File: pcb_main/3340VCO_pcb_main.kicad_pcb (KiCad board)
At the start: 2 copper layers, 80 x 114.5 mm, 75 parts, among them J1 MJ-352, J2 MJ-352, J3 MJ-352, J4 POWER_IN, J5 MJ-352, J6 MJ-352, J7 MJ-352, U1 NJM074, U2 NJM074, U3 V3340M

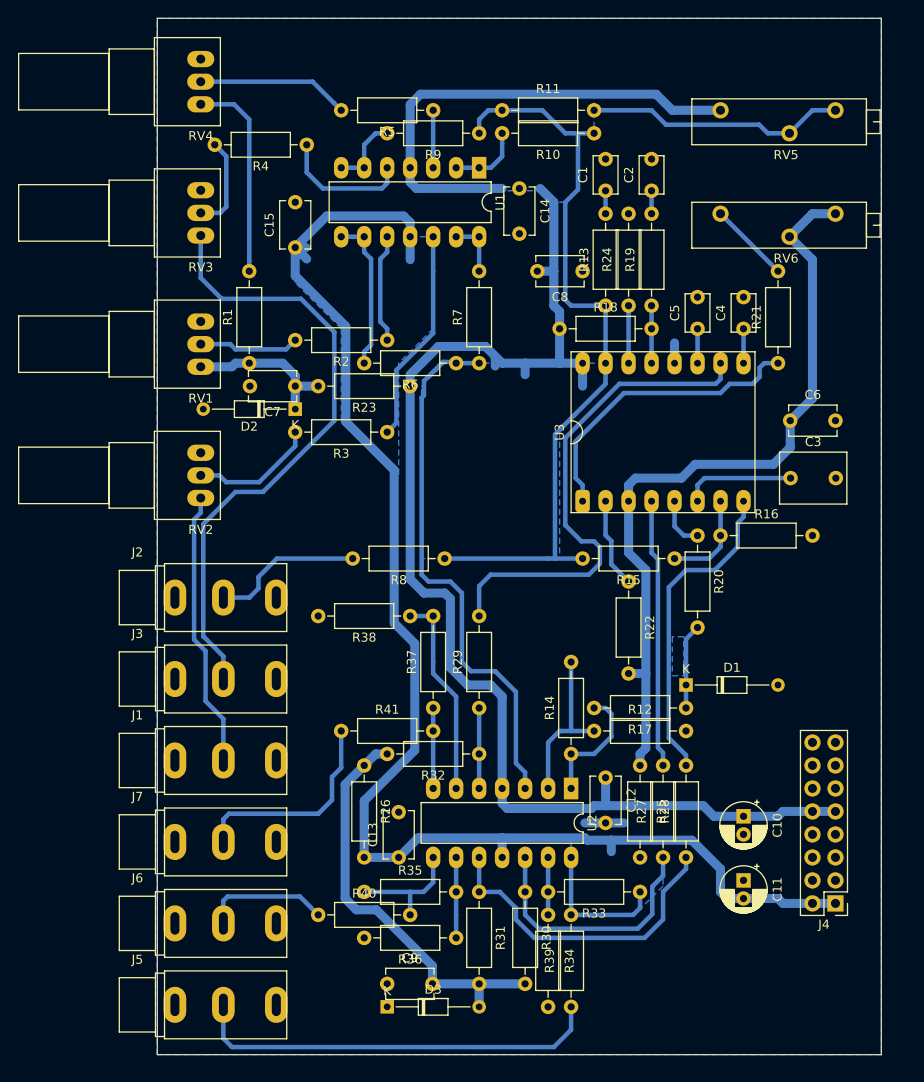
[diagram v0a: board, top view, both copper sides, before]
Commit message: pcb_main modify height: 114.5->109.5mm, optimize pad/drill diameter
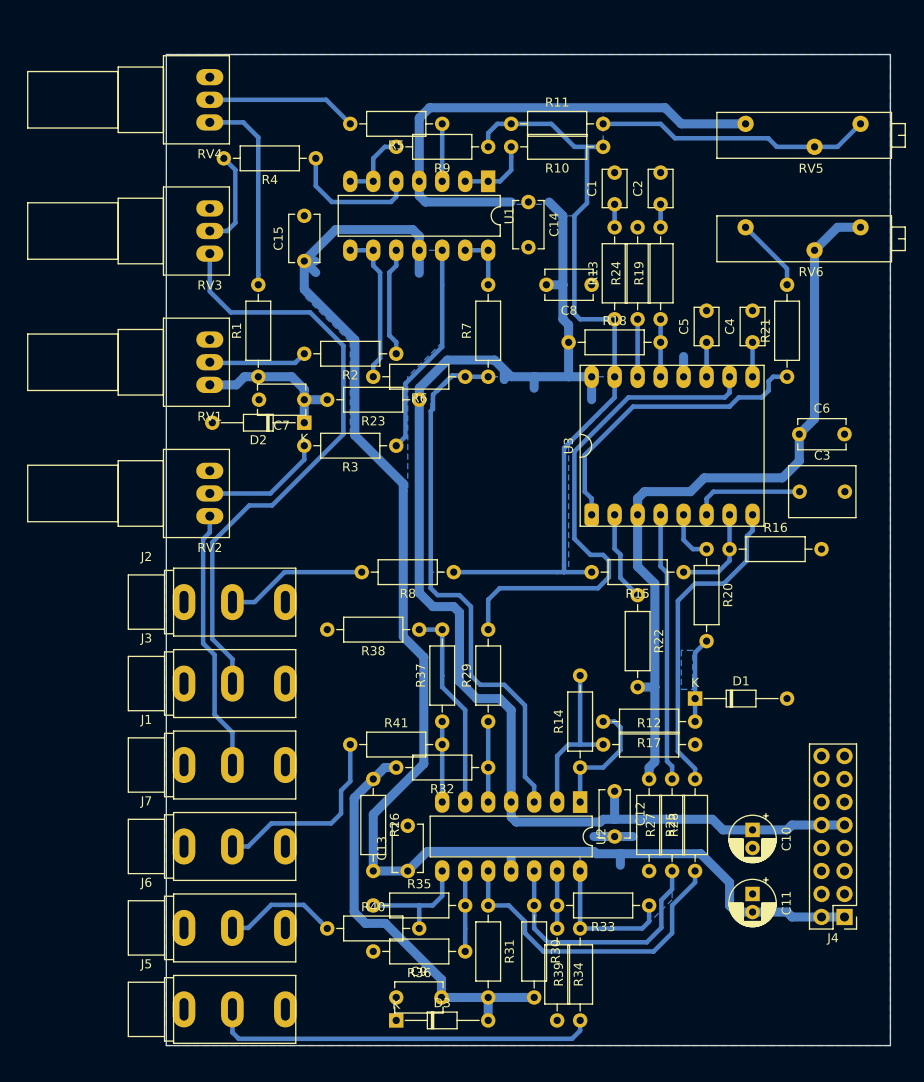
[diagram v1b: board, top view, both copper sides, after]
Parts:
- moved RV5 3.15 mm to (115.0, 61.7)
- moved RV6 3.15 mm to (115.0, 73.1)
- moved RV1 2.24 mm to (55.8, 85.5)
- moved RV2 2.24 mm to (55.8, 100.0)
- moved RV3 2.24 mm to (55.8, 71.0)
- moved RV4 2.24 mm to (55.8, 56.5)
- moved C1 1.80 mm to (100.5, 70.0)
- moved C10 1.80 mm to (115.8, 139.7)
- moved C11 1.80 mm to (115.8, 146.8)
- moved C12 1.80 mm to (100.5, 135.4)
- moved C13 1.80 mm to (77.7, 144.2)
- moved C14 1.80 mm to (91.0, 70.3)
- moved C15 1.80 mm to (66.2, 76.8)
- moved C2 1.80 mm to (105.6, 70.0)
- moved C3 1.80 mm to (121.0, 102.3)
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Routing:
- net Net-(J5-PadT): track 45.9 -> 42.8 mm
- net Net-(J7-PadT): track 23.4 -> 21.6 mm
- net Net-(J3-PadT): track 68.9 -> 67.1 mm
- net +12V: track 197.8 -> 199.5 mm
- net Net-(R11-Pad2): track 28.8 -> 30.5 mm
- net Net-(J1-PadT): track 30.6 -> 29.1 mm
- net Net-(J6-PadT): track 14.0 -> 12.6 mm
- net /VCO_VEE: track 85.0 -> 83.6 mm
- net Net-(J2-PadT): track 16.8 -> 15.7 mm
- net Net-(R21-Pad2): track 8.98 -> 8.25 mm
- net Net-(R4-Pad2): track 10.3 -> 10.9 mm
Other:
- board size 80 x 114.5 mm -> 80 x 109.5 mm

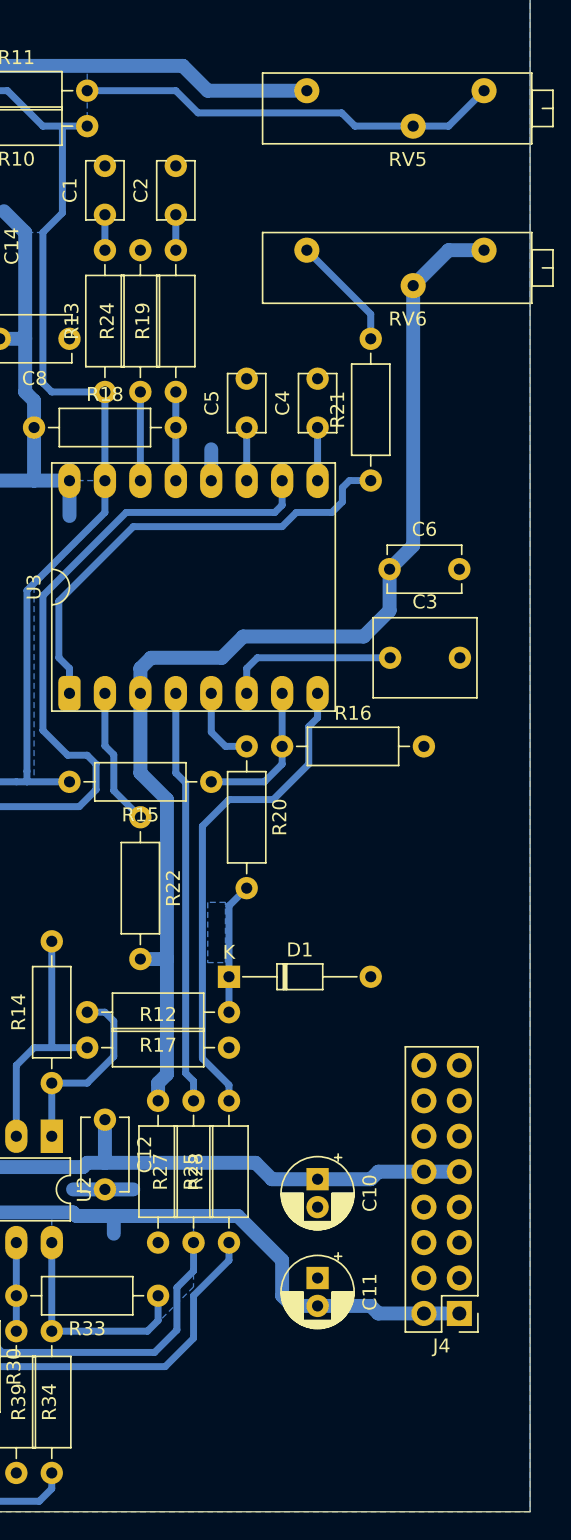
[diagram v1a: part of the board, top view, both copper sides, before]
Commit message: flip RV5 pin assign, add power source protection diode
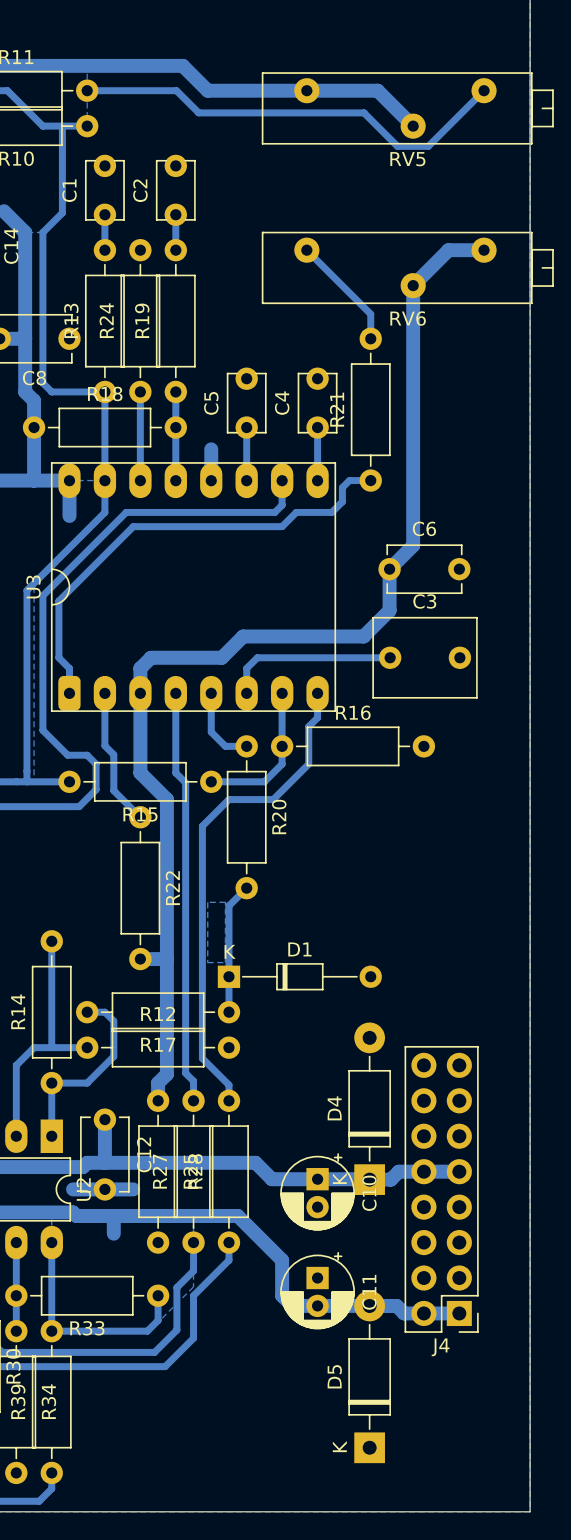
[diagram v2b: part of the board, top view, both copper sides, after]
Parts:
- added D4: 1N4007, Diode_THT:D_DO-41_SOD81_P10.16mm_Horizontal, F.Cu at (119.5, 139.7)
- added D5: 1N4007, Diode_THT:D_DO-41_SOD81_P10.16mm_Horizontal, F.Cu at (119.5, 158.9)
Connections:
- RV5 pad 2: Net-(R11-Pad2) -> +12V
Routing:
- net +12V: track 199.5 -> 208.2 mm
- net Net-(R11-Pad2): track 30.5 -> 31.7 mm

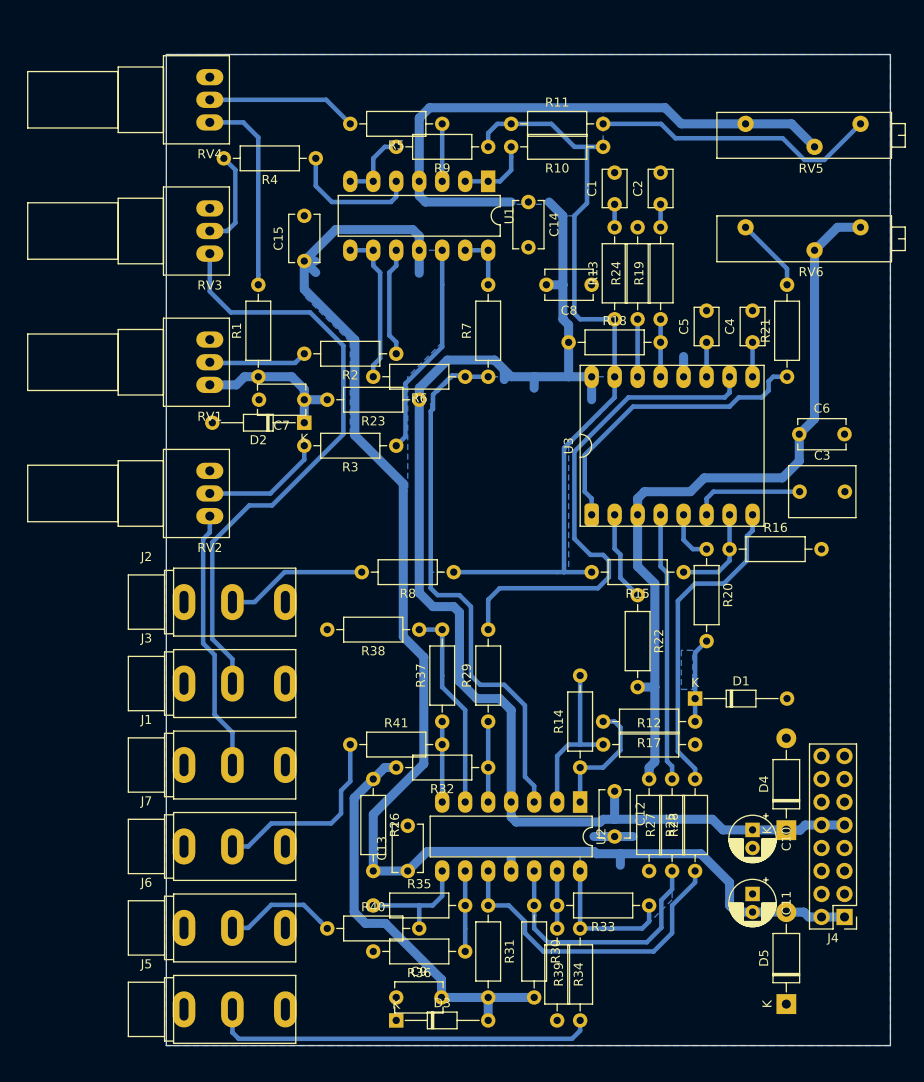
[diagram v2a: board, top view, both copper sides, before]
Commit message: redesign pcb_main for double-side
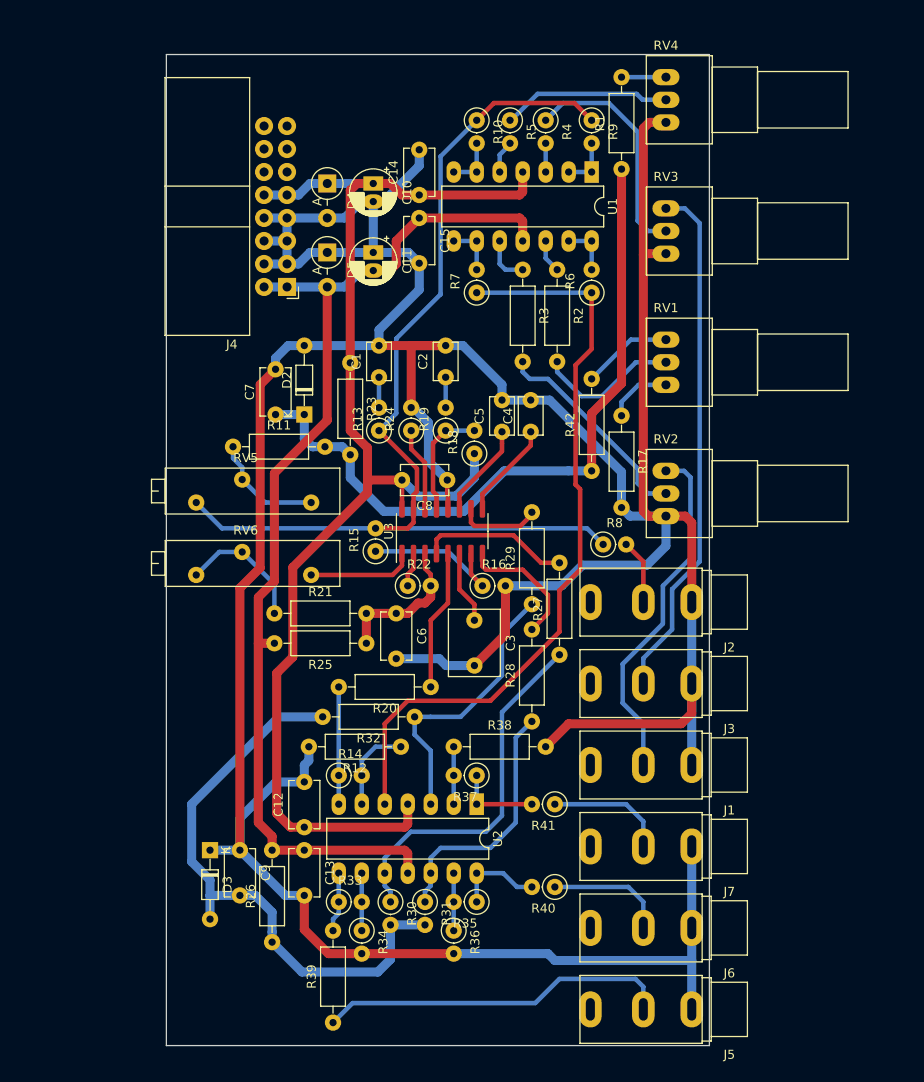
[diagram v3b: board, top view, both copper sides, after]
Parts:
- removed D1: 1N5231B, Diode_THT:D_DO-34_SOD68_P10.16mm_Horizontal
- added R42: 27k, Resistor_THT:R_Axial_DIN0207_L6.3mm_D2.5mm_P10.16mm_Horizontal, F.Cu at (98.0, 100.0)
- D2, D3: footprint Diode_THT:D_DO-34_SOD68_P10.16mm_Horizontal -> Diode_THT:D_DO-34_SOD68_P7.62mm_Horizontal
- D4, D5: footprint Diode_THT:D_DO-41_SOD81_P10.16mm_Horizontal -> Diode_THT:D_DO-41_SOD81_P3.81mm_Vertical_AnodeUp
- J4: footprint Connector_PinHeader_2.54mm:PinHeader_2x08_P2.54mm_Vertical -> Connector_IDC:IDC-Header_2x08_P2.54mm_Horizontal
- R10, R13, R14, R15, R16, R18, R19, R22, R24, R30, R31, R33, R34, R35, R36, R37, R4, R40, R41, R5, R6, R7, R8, R9: footprint Resistor_THT:R_Axial_DIN0207_L6.3mm_D2.5mm_P10.16mm_Horizontal -> Resistor_THT:R_Axial_DIN0207_L6.3mm_D2.5mm_P2.54mm_Vertical
- R11: value 200k -> 82k
- R17: value 1k -> 1.5k
- R25: value 820 -> 510
- R29: value 39k -> 3.9k
- RV5: value 100k -> 50k
- U3: footprint sop_conv:sop_conv_16pin -> Package_SO:SOIC-16_3.9x9.9mm_P1.27mm
- moved D5 97.3 mm to (68.8, 75.9), turned to 270 degrees
- moved J4 92.9 mm to (64.3, 79.7)
- moved D4 87.6 mm to (68.8, 68.2), turned to 270 degrees
- moved C10 82.8 mm to (73.9, 68.2)
- moved C11 82.3 mm to (73.9, 75.9)
- moved J1 68.4 mm to (115.2, 132.5), turned to 180 degrees
- moved J2 68.4 mm to (115.2, 114.5), turned to 180 degrees
- moved J3 68.4 mm to (115.2, 123.5), turned to 180 degrees
- moved J5 68.4 mm to (115.2, 159.5), turned to 180 degrees
- moved J6 68.4 mm to (115.2, 150.5), turned to 180 degrees
- moved J7 68.4 mm to (115.2, 141.5), turned to 180 degrees
- moved RV5 63.7 mm to (67.0, 103.5), turned to 0 degrees
- moved R21 62.4 mm to (62.9, 115.7), turned to 0 degrees
- moved RV6 61.5 mm to (67.0, 111.5), turned to 0 degrees
- moved RV1 50.6 mm to (106.2, 90.5), turned to 0 degrees
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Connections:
- C6 pad 1: /VCO_VEE -> VEE
- R11 pad 1: Net-(R10-Pad1) -> Net-(R11-Pad1)
- R11 pad 2: Net-(R11-Pad2) -> +5V
- R17 pad 1: Net-(D1-Pad1) -> Net-(R17-Pad1)
- R17 pad 2: Net-(R14-Pad1) -> GND
- R20 pad 2: Net-(D1-Pad1) -> Net-(R14-Pad1)
- R21 pad 2: Net-(R21-Pad2) -> VEE
- R22 pad 2: /VCO_VEE -> VEE
- R25 pad 1: /VCO_VEE -> VEE
- RV1 pad 1: GND -> Net-(R17-Pad1)
- RV1 pad 3: +5V -> Net-(R42-Pad2)
- RV3 pad 2: Net-(R4-Pad2) -> Net-(R4-Pad1)
- RV4 pad 2: Net-(R5-Pad2) -> Net-(R5-Pad1)
- RV5 pad 1: +12V -> Net-(R11-Pad1)
- RV5 pad 2: +12V -> Net-(R11-Pad1)
- RV5 pad 3: Net-(R11-Pad2) -> Net-(R10-Pad1)
- RV6 pad 1: Net-(R21-Pad2) -> Net-(RV6-Pad1)
- RV6 pad 2: /VCO_VEE -> Net-(R21-Pad1)
- RV6 pad 3: /VCO_VEE -> Net-(R21-Pad1)
- U1 pad 1: Net-(R10-Pad2) -> Net-(R9-Pad2)
- U1 pad 10: Net-(R2-Pad1) -> Net-(R3-Pad1)
- U1 pad 12: Net-(R3-Pad1) -> Net-(R2-Pad1)
- U1 pad 13: Net-(R7-Pad2) -> Net-(R6-Pad2)
- U1 pad 14: Net-(R7-Pad2) -> Net-(R6-Pad2)
- U1 pad 2: Net-(R10-Pad2) -> Net-(R9-Pad2)
- U1 pad 3: Net-(R5-Pad1) -> Net-(R4-Pad2)
- U1 pad 5: Net-(R4-Pad1) -> Net-(R5-Pad2)
- U1 pad 6: Net-(R9-Pad2) -> Net-(R10-Pad2)
- U1 pad 7: Net-(R9-Pad2) -> Net-(R10-Pad2)
- U1 pad 8: Net-(R6-Pad2) -> Net-(R7-Pad2)
- U1 pad 9: Net-(R6-Pad2) -> Net-(R7-Pad2)
- U2 pad 1: Net-(R14-Pad1) -> Net-(R37-Pad1)
- U2 pad 10: Net-(R28-Pad1) -> Net-(R27-Pad1)
- U2 pad 12: Net-(R27-Pad1) -> Net-(R28-Pad1)
- U2 pad 13: Net-(R33-Pad2) -> Net-(R35-Pad2)
- U2 pad 14: Net-(R33-Pad1) -> Net-(R35-Pad1)
- U2 pad 2: Net-(R12-Pad1) -> Net-(R37-Pad2)
- U2 pad 3: Net-(R6-Pad1) -> Net-(R29-Pad1)
- U2 pad 5: Net-(R29-Pad1) -> Net-(R6-Pad1)
- U2 pad 6: Net-(R37-Pad2) -> Net-(R12-Pad1)
- U2 pad 7: Net-(R37-Pad1) -> Net-(R14-Pad1)
- U2 pad 8: Net-(R35-Pad1) -> Net-(R33-Pad1)
- U2 pad 9: Net-(R35-Pad2) -> Net-(R33-Pad2)
- U3 pad 1: Net-(R21-Pad1) -> Net-(RV6-Pad1)
- U3 pad 3: /VCO_VEE -> VEE
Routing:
- net GND: track 6.57 -> 436.1 mm
- net /VCO_VEE: track 83.6 -> 0.00 mm
- net +12V: track 208.2 -> 145.4 mm
- net +5V: track 17.6 -> 79.0 mm
- net Net-(R29-Pad2): track 55.6 -> 9.19 mm
- net -12V: track 157.7 -> 120.7 mm
- net Net-(R11-Pad2): track 31.7 -> 0.00 mm
- net Net-(R10-Pad1): track 84.9 -> 116.4 mm
- net Net-(R6-Pad1): track 59.8 -> 84.5 mm
- net Net-(R29-Pad1): track 8.89 -> 31.2 mm
- net Net-(R28-Pad2): track 35.3 -> 14.5 mm
- net -5V: track 46.1 -> 65.6 mm
- net Net-(R21-Pad1): track 33.5 -> 14.4 mm
- net Net-(R3-Pad1): track 23.7 -> 5.34 mm
- net Net-(R1-Pad2): track 22.3 -> 4.91 mm
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- removed copper zone on B.Cu, net +12V
- removed copper zone on B.Cu, net -12V
- removed copper zone on B.Cu, net GND
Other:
- board size 80 x 109.5 mm -> 60 x 109.5 mm

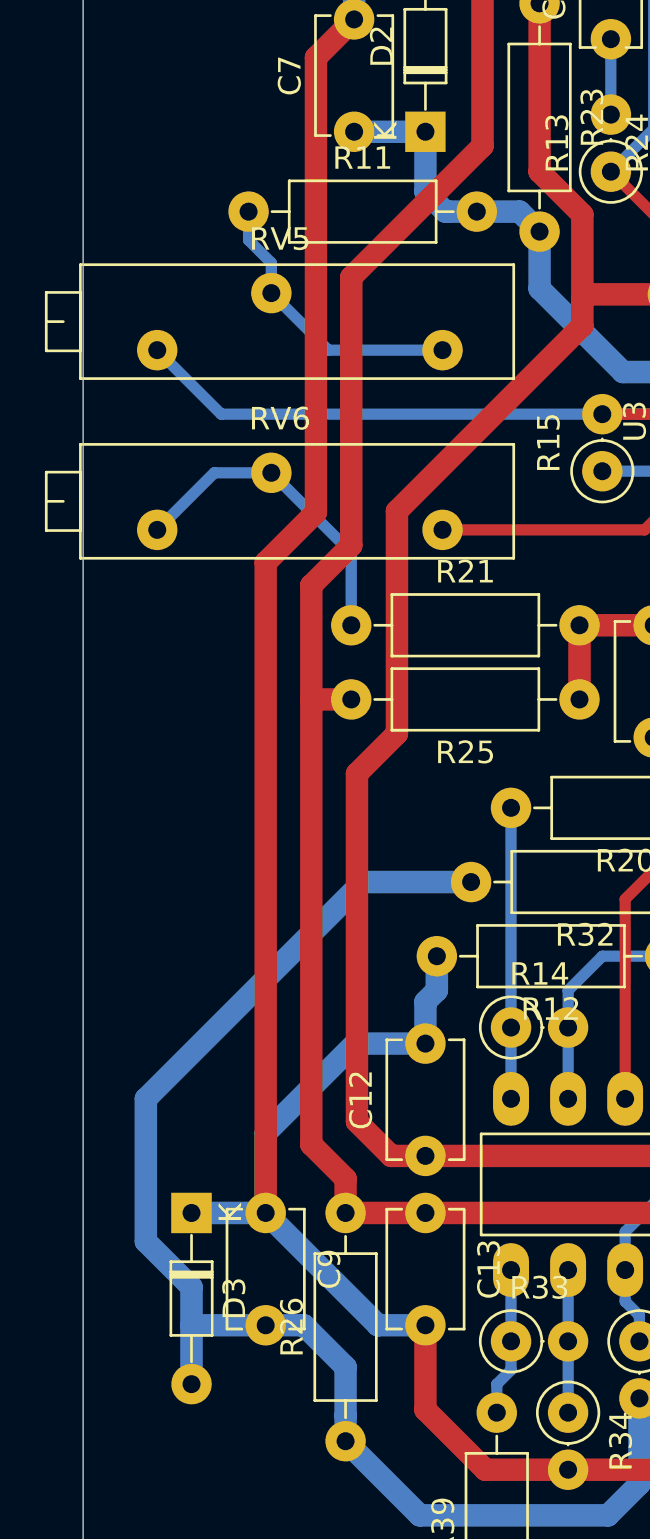
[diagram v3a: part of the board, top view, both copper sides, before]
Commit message: tweak pcb_main, adjust frontpanel horizontal position
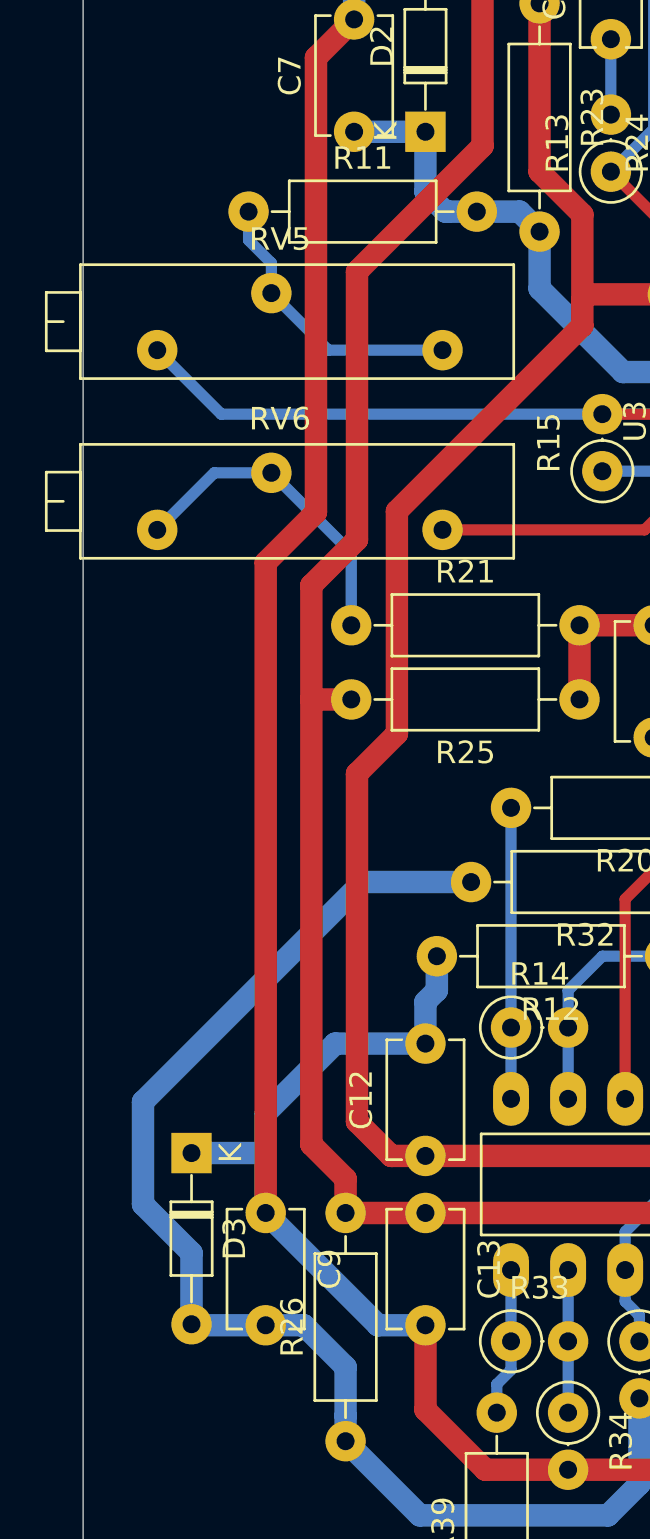
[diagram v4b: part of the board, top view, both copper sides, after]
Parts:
- moved D3 2.67 mm to (55.8, 139.2)
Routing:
- net -5V: track 65.6 -> 63.1 mm
- net GND: track 436.1 -> 436.6 mm
